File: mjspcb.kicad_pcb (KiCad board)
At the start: 2 copper layers, 97.2 x 55.9 mm, 78 parts, among them P1 Batteries, P10 Lipo, P2 serial breakout, P3 I2C breakout, P4 GPS, P5 piezo, P6 BPW34, P7 electrodes, P8 perfboard breakout, P9 reset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

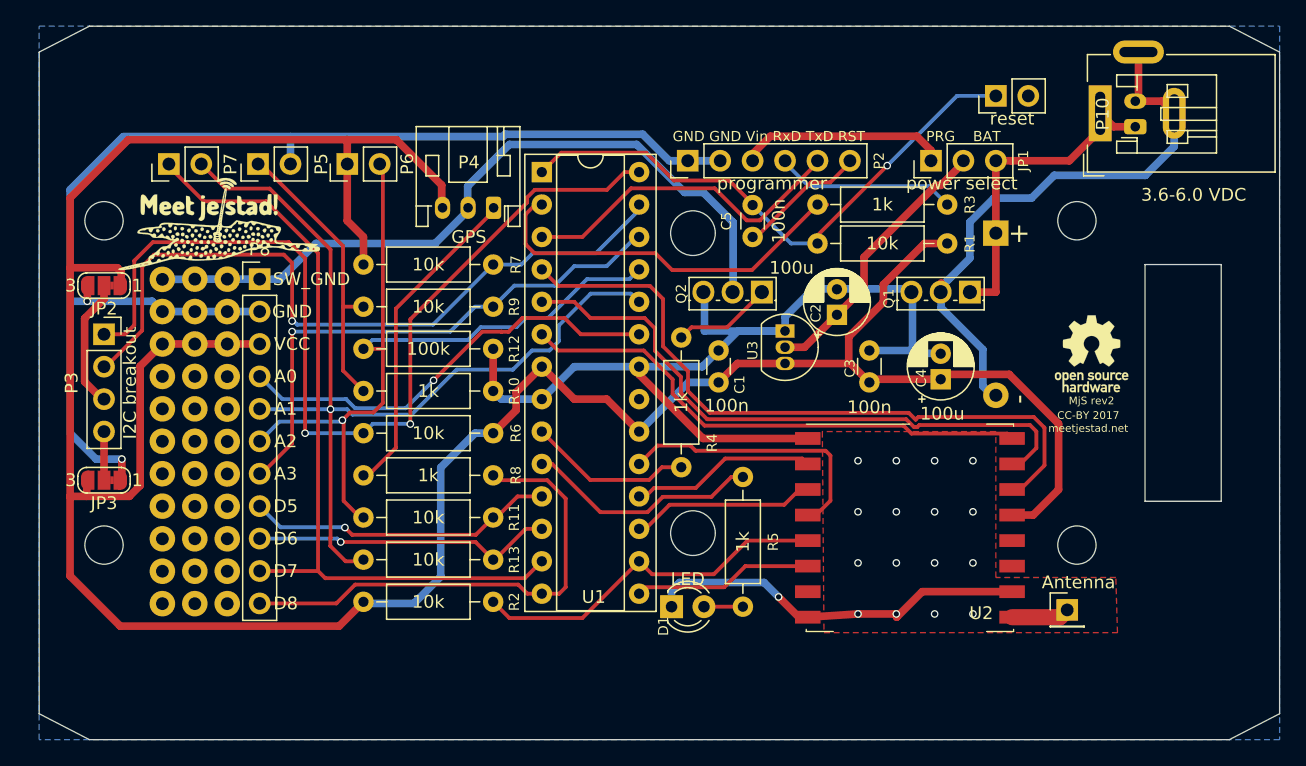
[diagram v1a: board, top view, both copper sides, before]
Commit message: Replace I²C connector with a more sturdy one
This one has extra holes to plug in the sensor, so it can be mounted
lower and more stable. This also makes the board slightly longer at the
bottom to accomdate the new connector, and shorter at the top.
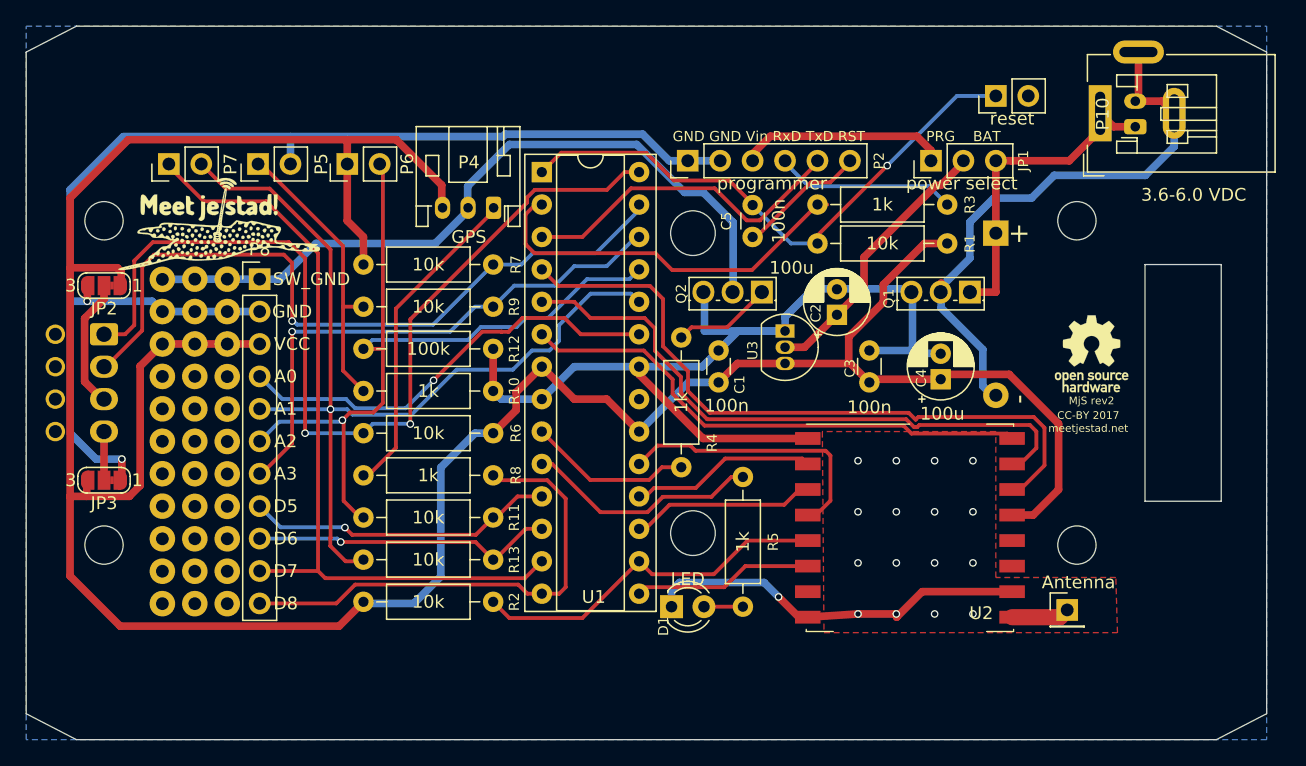
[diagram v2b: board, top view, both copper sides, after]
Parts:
- P3: footprint Connector_PinSocket_2.54mm:PinSocket_1x04_P2.54mm_Vertical -> meetjestad:Molex_KK-254_44812-0004_1x04_P2.54mm_Vertical; moved to B.Cu
- turned P3 to 270 degrees
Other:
- outline, holes or cut-outs redrawn
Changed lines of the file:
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@@
     (pad_to_mask_clearance 0)
     (solder_mask_min_width 0.25)
-    (aux_axis_origin 121.793 148.59)
-    (grid_origin 134.62 148.59)
+    (aux_axis_origin 133.604 148.59)
+    (grid_origin 133.604 148.59)
     (visible_elements 7FFFFF7F)
     (pcbplotparams
@@
     (add_net VIN)
   )
-  (module Connector_PinSocket_2.54mm:PinSocket_1x04_P2.54mm_Vertical (layer F.Cu)
-    (at 139.7 116.84)
-    (descr "Through hole straight socket strip, 1x04, 2.54mm pitch, single row (from Kicad 4.0.7), script generated")
-    (tags "Through hole socket strip THT 1x04 2.54mm single row")
-    (fp_text reference P3 (at -2.54 3.81 90) (layer F.SilkS)
-      (effects (font (size 1 1) (thickness 0.15)))
+  (module meetjestad:Molex_KK-254_44812-0004_1x04_P2.54mm_Vertical (layer B.Cu)
+    (at 139.7 116.84 270)
+    (descr "Molex KK-254 Interconnect System, old/engineering part number: AE-6410-04A example for new part number: 22-27-2041, 4 Pins (http://www.molex.com/pdm_docs/sd/022272021_sd.pdf), generated with kicad-footprint-generator")
+    (tags "connector Molex KK-254 side entry")
+    (fp_text reference P3 (at 3.81 6.35 270) (layer B.SilkS)
+      (effects (font (size 1 1) (thickness 0.15)) (justify mirror))
     )
-    (fp_text value "I2C breakout" (at 2.032 3.81 90) (layer F.SilkS)
-      (effects (font (size 1 1) (thickness 0.15)))
+    (fp_text value "I2C breakout" (at 3.81 -3.7084 270) (layer B.Fab)
+      (effects (font (size 1 1) (thickness 0.15)) (justify mirror))
     )
-    (fp_line (start -1.27 -1.27) (end 0.635 -1.27) (layer F.Fab) (width 0.1))
-    (fp_line (start 0.635 -1.27) (end 1.27 -0.635) (layer F.Fab) (width 0.1))
-    (fp_line (start 1.27 -0.635) (end 1.27 8.89) (layer F.Fab) (width 0.1))
-    (fp_line (start 1.27 8.89) (end -1.27 8.89) (layer F.Fab) (width 0.1))
-    (fp_line (start -1.27 8.89) (end -1.27 -1.27) (layer F.Fab) (width 0.1))
-    (fp_line (start -1.33 1.27) (end 1.33 1.27) (layer F.SilkS) (width 0.12))
-    (fp_line (start -1.33 1.27) (end -1.33 8.95) (layer F.SilkS) (width 0.12))
-    (fp_line (start -1.33 8.95) (end 1.33 8.95) (layer F.SilkS) (width 0.12))
-    (fp_line (start 1.33 1.27) (end 1.33 8.95) (layer F.SilkS) (width 0.12))
-    (fp_line (start 1.33 -1.33) (end 1.33 0) (layer F.SilkS) (width 0.12))
-    (fp_line (start 0 -1.33) (end 1.33 -1.33) (layer F.SilkS) (width 0.12))
-    (fp_line (start -1.8 -1.8) (end 1.75 -1.8) (layer F.CrtYd) (width 0.05))
-    (fp_line (start 1.75 -1.8) (end 1.75 9.4) (layer F.CrtYd) (width 0.05))
-    (fp_line (start 1.75 9.4) (end -1.8 9.4) (layer F.CrtYd) (width 0.05))
-    (fp_line (start -1.8 9.4) (end -1.8 -1.8) (layer F.CrtYd) (width 0.05))
-    (fp_text user %R (at 0 3.81 90) (layer F.Fab)
-      (effects (font (size 1 1) (thickness 0.15)))
+    (fp_line (start -2.032 5.6896) (end 1.238 5.6896) (layer B.SilkS) (width 0.12))
+    (fp_line (start 9.398 5.4356) (end -1.778 5.4356) (layer B.SilkS) (width 0.12))
+    (fp_line (start 8.42 -2.3114) (end 9.398 -2.3114) (layer B.SilkS) (width 0.12))
+    (fp_line (start 6.82 -1.7114) (end 8.42 -1.7114) (layer B.SilkS) (width 0.12))
+    (fp_line (start 5.88 -2.3114) (end 6.82 -2.3114) (layer B.SilkS) (width 0.12))
+    (fp_line (start 4.28 -1.7114) (end 5.88 -1.7114) (layer B.SilkS) (width 0.12))
+    (fp_line (start 3.34 -2.3114) (end 4.28 -2.3114) (layer B.SilkS) (width 0.12))
+    (fp_line (start 1.74 -1.7114) (end 3.34 -1.7114) (layer B.SilkS) (width 0.12))
+    (fp_line (start 0.8 -2.3114) (end 1.74 -2.3114) (layer B.SilkS) (width 0.12))
+    (fp_line (start -0.8 -1.7114) (end 0.8 -1.7114) (layer B.SilkS) (width 0.12))
+    (fp_line (start -1.778 -2.3114) (end -0.8 -2.3114) (layer B.SilkS) (width 0.12))
+    (fp_line (start -1.651 5.3086) (end -1.651 -2.1844) (layer B.Fab) (width 0.1))
+    (fp_line (start -1.651 -2.1844) (end 9.271 -2.1844) (layer B.Fab) (width 0.1))
+    (fp_line (start 9.271 -2.1844) (end 9.271 5.3086) (layer B.Fab) (width 0.1))
+    (fp_line (start -1.651 5.3086) (end 9.271 5.3086) (layer B.Fab) (width 0.1))
+    (fp_line (start -1.778 5.4356) (end -1.778 -2.3114) (layer B.SilkS) (width 0.12))
+    (fp_line (start 9.398 5.4356) (end 9.398 -2.3114) (layer B.SilkS) (width 0.12))
+    (fp_line (start -2.032 5.6896) (end -2.032 2.4196) (layer B.SilkS) (width 0.12))
+    (fp_line (start -1.27 0.5) (end -0.562893 0) (layer B.Fab) (width 0.1))
+    (fp_line (start -0.562893 0) (end -1.27 -0.5) (layer B.Fab) (width 0.1))
+    (fp_line (start -0.8 -1.7114) (end -0.8 -2.3114) (layer B.SilkS) (width 0.12))
+    (fp_line (start 0.8 -2.3114) (end 0.8 -1.7114) (layer B.SilkS) (width 0.12))
+    (fp_line (start 1.74 -1.7114) (end 1.74 -2.3114) (layer B.SilkS) (width 0.12))
+    (fp_line (start 3.34 -2.3114) (end 3.34 -1.7114) (layer B.SilkS) (width 0.12))
+    (fp_line (start 4.28 -1.7114) (end 4.28 -2.3114) (layer B.SilkS) (width 0.12))
+    (fp_line (start 5.88 -2.3114) (end 5.88 -1.7114) (layer B.SilkS) (width 0.12))
+    (fp_line (start 6.82 -1.7114) (end 6.82 -2.3114) (layer B.SilkS) (width 0.12))
+    (fp_line (start 8.42 -2.3114) (end 8.42 -1.7114) (layer B.SilkS) (width 0.12))
+    (fp_line (start -2.15 5.81) (end -2.15 -2.69) (layer B.CrtYd) (width 0.05))
+    (fp_line (start -2.15 -2.69) (end 9.77 -2.69) (layer B.CrtYd) (width 0.05))
+    (fp_line (start 9.77 -2.69) (end 9.77 5.81) (layer B.CrtYd) (width 0.05))
+    (fp_line (start 9.77 5.81) (end -2.15 5.81) (layer B.CrtYd) (width 0.05))
+    (fp_text user %R (at 3.81 1.905 270) (layer B.Fab)
+      (effects (font (size 1 1) (thickness 0.15)) (justify mirror))
     )
-    (pad 1 thru_hole rect (at 0 0) (size 1.7 1.7) (drill 1) (layers *.Cu *.Mask)
+    (pad 1 thru_hole roundrect (at 0 0 270) (size 1.74 2.2) (drill 1.2) (layers *.Cu *.Mask) (roundrect_rratio 0.143678)
       (net 11 SCL))
-    (pad 2 thru_hole oval (at 0 2.54) (size 1.7 1.7) (drill 1) (layers *.Cu *.Mask)
+    (pad 2 thru_hole oval (at 2.54 0 270) (size 1.74 2.2) (drill 1.2) (layers *.Cu *.Mask)
       (net 10 SDA))
-    (pad 3 thru_hole oval (at 0 5.08) (size 1.7 1.7) (drill 1) (layers *.Cu *.Mask)
+    (pad 3 thru_hole oval (at 5.08 0 270) (size 1.74 2.2) (drill 1.2) (layers *.Cu *.Mask)
       (net 42 "Net-(JP2-Pad2)"))
-    (pad 4 thru_hole oval (at 0 7.62) (size 1.7 1.7) (drill 1) (layers *.Cu *.Mask)
+    (pad 4 thru_hole oval (at 7.62 0 270) (size 1.74 2.2) (drill 1.2) (layers *.Cu *.Mask)
       (net 43 "Net-(JP3-Pad2)"))
-    (model ${KISYS3DMOD}/Connector_PinSocket_2.54mm.3dshapes/PinSocket_1x04_P2.54mm_Vertical.wrl
+    (pad "" np_thru_hole circle (at 0 3.81 270) (size 1.524 1.524) (drill 1.016) (layers *.Cu *.Mask))
+    (pad "" np_thru_hole circle (at 2.54 3.81 270) (size 1.524 1.524) (drill 1.016) (layers *.Cu *.Mask))
+    (pad "" np_thru_hole circle (at 5.08 3.81 270) (size 1.524 1.524) (drill 1.016) (layers *.Cu *.Mask))
+    (pad "" np_thru_hole circle (at 7.62 3.81 270) (size 1.524 1.524) (drill 1.016) (layers *.Cu *.Mask))
+    (model ${KISYS3DMOD}/Connector_Molex.3dshapes/Molex_KK-254_AE-6410-04A_1x04_P2.54mm_Vertical.wrl
       (at (xyz 0 0 0))
       (scale (xyz 1 1 1))
@@
   (gr_line (start 221.234 111.379) (end 227.203 111.379) (layer Edge.Cuts) (width 0.1))
   (gr_line (start 227.203 129.921) (end 221.234 129.921) (layer Edge.Cuts) (width 0.1))
-  (gr_line (start 138.557 148.59) (end 134.62 146.558) (layer Edge.Cuts) (width 0.1))
-  (gr_line (start 138.557 92.71) (end 134.62 94.742) (layer Edge.Cuts) (width 0.1))
-  (gr_line (start 231.775 94.742) (end 227.838 92.71) (layer Edge.Cuts) (width 0.1))
-  (gr_line (start 231.775 146.558) (end 227.838 148.59) (layer Edge.Cuts) (width 0.1))
+  (gr_line (start 137.541 148.59) (end 133.604 146.558) (layer Edge.Cuts) (width 0.1))
+  (gr_line (start 137.541 92.71) (end 133.604 94.742) (layer Edge.Cuts) (width 0.1))
+  (gr_line (start 230.759 94.742) (end 226.822 92.71) (layer Edge.Cuts) (width 0.1))
+  (gr_line (start 230.759 146.558) (end 226.822 148.59) (layer Edge.Cuts) (width 0.1))
   (gr_text "GND GND Vin RxD TxD RST" (at 191.77 101.346) (layer F.SilkS)
     (effects (font (size 0.8 0.8) (thickness 0.1)))
@@
     (effects (font (size 1 1) (thickness 0.15)) (justify mirror))
   )
-  (gr_line (start 227.838 148.59) (end 138.557 148.59) (layer Edge.Cuts) (width 0.1))
-  (gr_line (start 231.775 94.742) (end 231.775 146.558) (layer Edge.Cuts) (width 0.1))
-  (gr_line (start 138.557 92.71) (end 227.838 92.71) (layer Edge.Cuts) (width 0.1))
-  (gr_line (start 134.62 146.558) (end 134.62 94.742) (layer Edge.Cuts) (width 0.1))
+  (gr_line (start 226.822 148.59) (end 137.541 148.59) (layer Edge.Cuts) (width 0.1))
+  (gr_line (start 230.759 94.742) (end 230.759 146.558) (layer Edge.Cuts) (width 0.1))
+  (gr_line (start 137.541 92.71) (end 226.822 92.71) (layer Edge.Cuts) (width 0.1))
+  (gr_line (start 133.604 146.558) (end 133.604 94.742) (layer Edge.Cuts) (width 0.1))
   (gr_text programmer (at 192.024 105.029) (layer F.SilkS)
     (effects (font (size 1 1) (thickness 0.1)))
@@
     (polygon
       (pts
-        (xy 134.62 92.71) (xy 231.775 92.71) (xy 231.775 148.59) (xy 134.62 148.59)
+        (xy 133.604 92.71) (xy 230.759 92.71) (xy 230.759 148.59) (xy 133.604 148.59)
       )
     )
@@
     (polygon
       (pts
-        (xy 231.521 148.336) (xy 231.521 93.0275) (xy 212.217 92.86875) (xy 212.217 148.17725)
+        (xy 230.505 148.336) (xy 230.505 92.964) (xy 212.217 92.964) (xy 212.217 148.336)
       )
     )

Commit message: Replace 2-pin sensor connectors with KK254
These are latching, polarity protected connectors. This mostly changes
to silkscreen, though the pads are also slighly differently sized.
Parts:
- P5, P6, P7: footprint Connector_PinHeader_2.54mm:PinHeader_1x02_P2.54mm_Vertical -> Connector_Molex:Molex_KK-254_AE-6410-02A_1x02_P2.54mm_Vertical
- turned P5 to 0 degrees
- turned P6 to 0 degrees
- turned P7 to 0 degrees

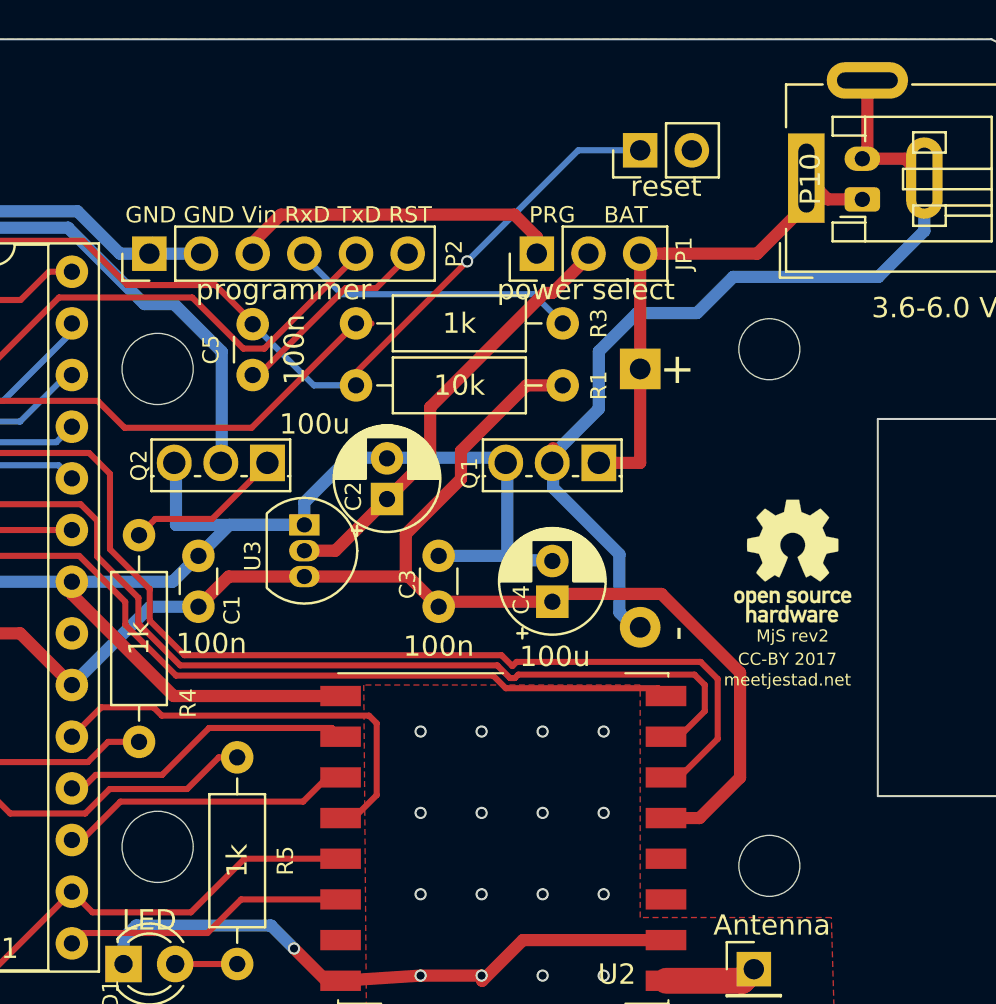
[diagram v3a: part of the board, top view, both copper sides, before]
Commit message: Move reset header to fix connections
This was accidentally disconnected when introducing a keepout zone for
the antennas recently.
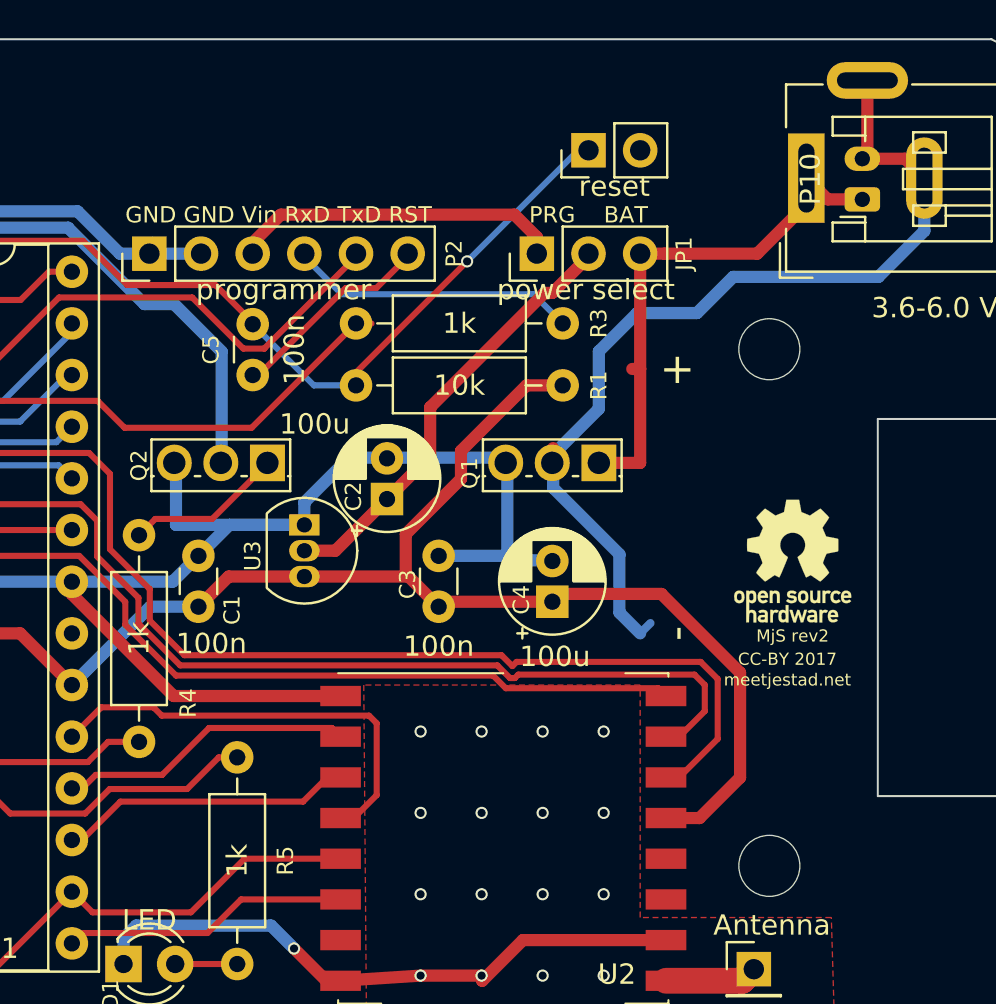
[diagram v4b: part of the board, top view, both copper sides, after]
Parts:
- removed P1: Batteries, Battery:BatteryHolder_Keystone_2479_3xAAA
- moved P9 2.54 mm to (207.0, 98.2)
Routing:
- net RST: track 44.6 -> 42.0 mm
